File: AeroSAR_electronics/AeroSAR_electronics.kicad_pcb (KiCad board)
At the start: 2 copper layers, 53.5 x 53 mm, 1 part

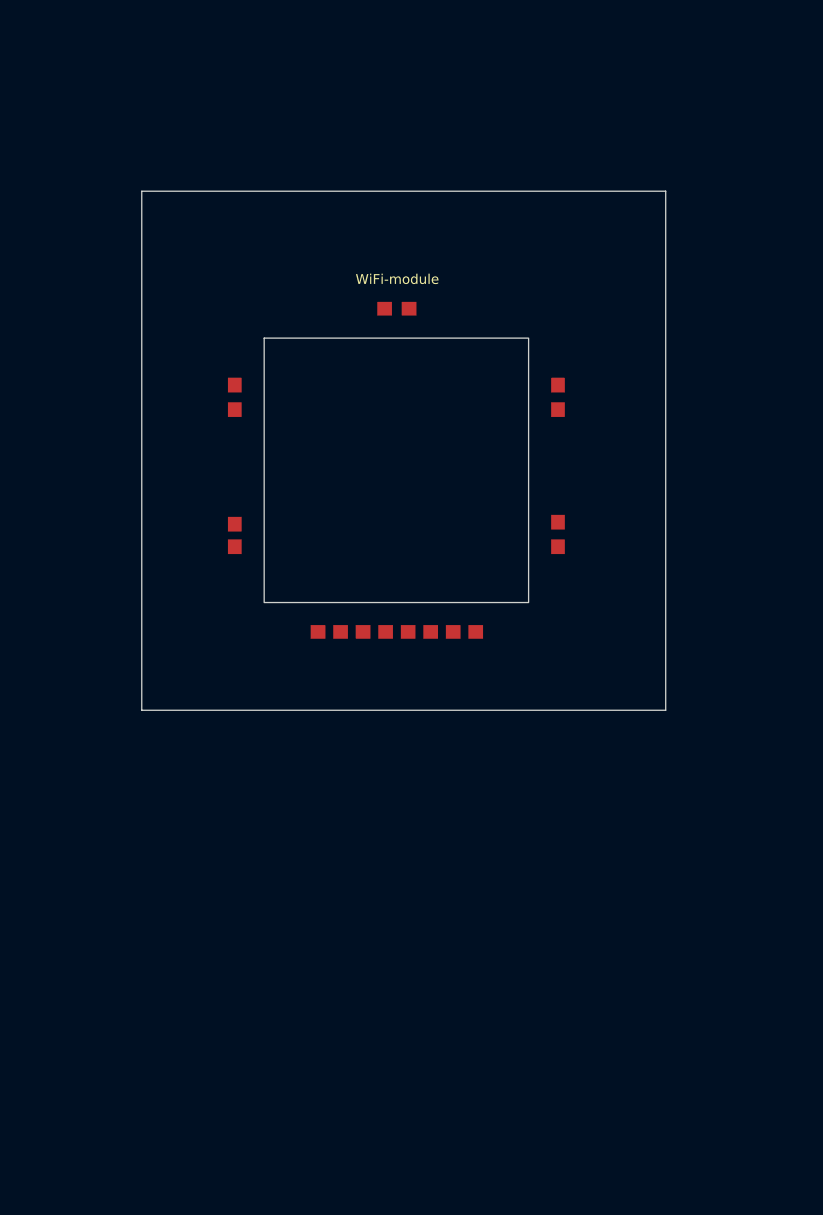
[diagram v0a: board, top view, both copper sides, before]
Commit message: Rearranged the FC-top schematic pins & created a basic pcb outline
Edited the pin type for most of the ground pins
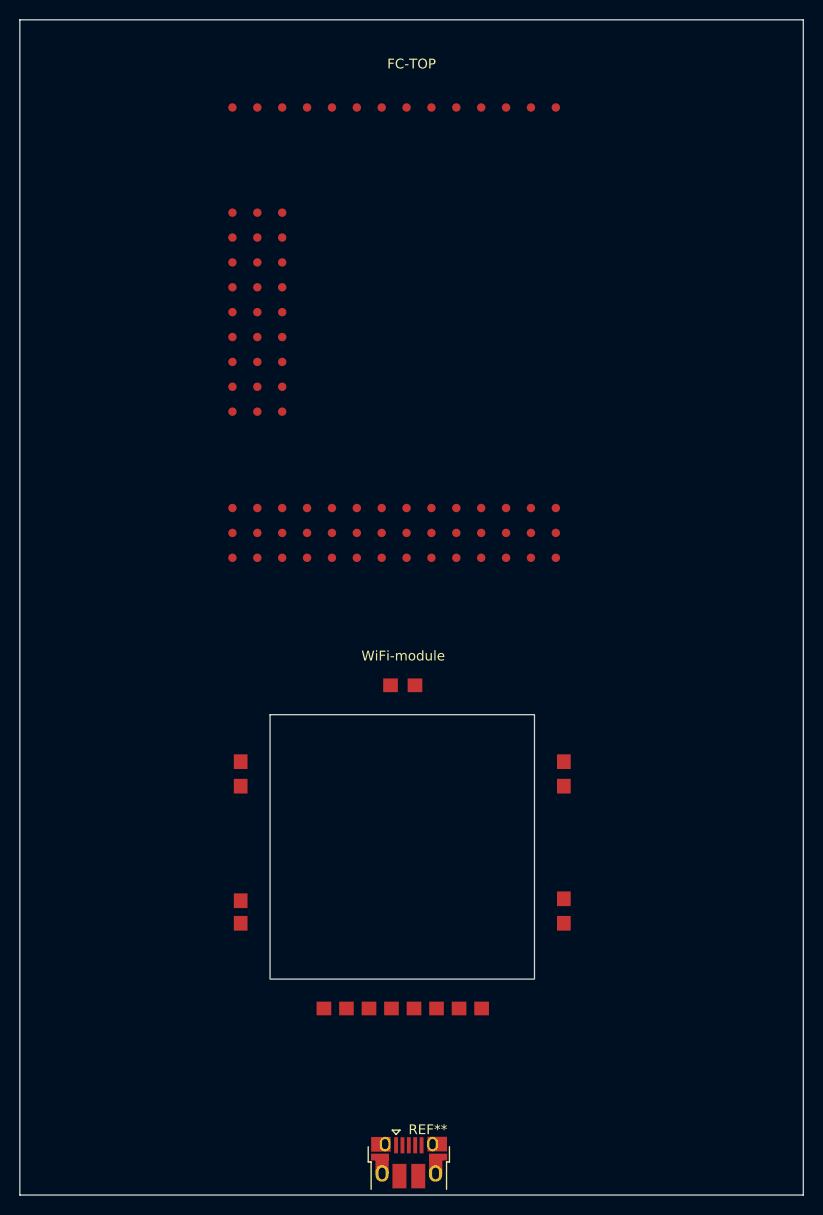
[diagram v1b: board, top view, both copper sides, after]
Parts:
- added FC-TOP: H743-WING-Top, Flight_Controller_Top:H743-WING_TOP, F.Cu at (118.8, 53.9)
- added REF**: USB_Micro-B_Amphenol_10103594-0001LF_Horizontal, Connector_USB:USB_Micro-B_Amphenol_10103594-0001LF_Horizontal, F.Cu at (138.3, 163.2)
- moved WiFi-module 38.5 mm to (121.6, 115.0)
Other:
- board size 53.5 x 53 mm -> 80 x 120 mm

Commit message: Prepared v1 of the schematic
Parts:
- moved REF** 220.0 mm to (357.5, 144.1)
- moved WiFi-module 220.0 mm to (340.8, 95.8)
- moved FC-TOP 220.0 mm to (338.0, 34.8)
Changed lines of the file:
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@@
 	(footprint "Connector_USB:USB_Micro-B_Amphenol_10103594-0001LF_Horizontal"
 		(layer "F.Cu")
-		(at 138.295 163.185)
+		(at 357.495 144.085)
 		(descr "Micro USB Type B 10103594-0001LF, http://cdn.amphenol-icc.com/media/wysiwyg/files/drawing/10103594.pdf")
 		(tags "USB USB_B USB_micro USB_OTG")
@@
 	(footprint "BL-M8812EU2:BL-M8812EU2"
 		(layer "F.Cu")
-		(at 121.6 114.95)
+		(at 340.8 95.85)
 		(property "Reference" "WiFi-module"
 			(at 16.1 -3.5 0)
@@
 	(footprint "Flight_Controller_Top:H743-WING_TOP"
 		(layer "F.Cu")
-		(at 118.8 53.85)
+		(at 338 34.75)
 		(property "Reference" "FC-TOP"
 			(at 19.75 -2.85 0)
@@
 	)
 	(gr_rect
-		(start 98.55 46.5)
-		(end 178.55 166.5)
+		(start 317.75 27.4)
+		(end 397.75 147.4)
 		(stroke
 			(width 0.05)

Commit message: Fixed footprint not loading on schematic and replaced the usb A with usb micro
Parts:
- moved FC-TOP 217.9 mm to (120.4, 46.0)
- moved WiFi-module 217.7 mm to (123.5, 108.5)
- moved REF** 217.7 mm to (140.1, 156.7)
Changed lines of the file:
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@@
 	(footprint "Connector_USB:USB_Micro-B_Amphenol_10103594-0001LF_Horizontal"
 		(layer "F.Cu")
-		(at 357.495 144.085)
+		(at 140.145 156.685)
 		(descr "Micro USB Type B 10103594-0001LF, http://cdn.amphenol-icc.com/media/wysiwyg/files/drawing/10103594.pdf")
 		(tags "USB USB_B USB_micro USB_OTG")
@@
 	(footprint "BL-M8812EU2:BL-M8812EU2"
 		(layer "F.Cu")
-		(at 340.8 95.85)
+		(at 123.45 108.45)
 		(property "Reference" "WiFi-module"
 			(at 16.1 -3.5 0)
@@
 	(footprint "Flight_Controller_Top:H743-WING_TOP"
 		(layer "F.Cu")
-		(at 338 34.75)
+		(at 120.4 46.05)
 		(property "Reference" "FC-TOP"
 			(at 19.75 -2.85 0)
@@
 	)
 	(gr_rect
-		(start 317.75 27.4)
-		(end 397.75 147.4)
+		(start 100.4 40)
+		(end 180.4 160)
 		(stroke
 			(width 0.05)

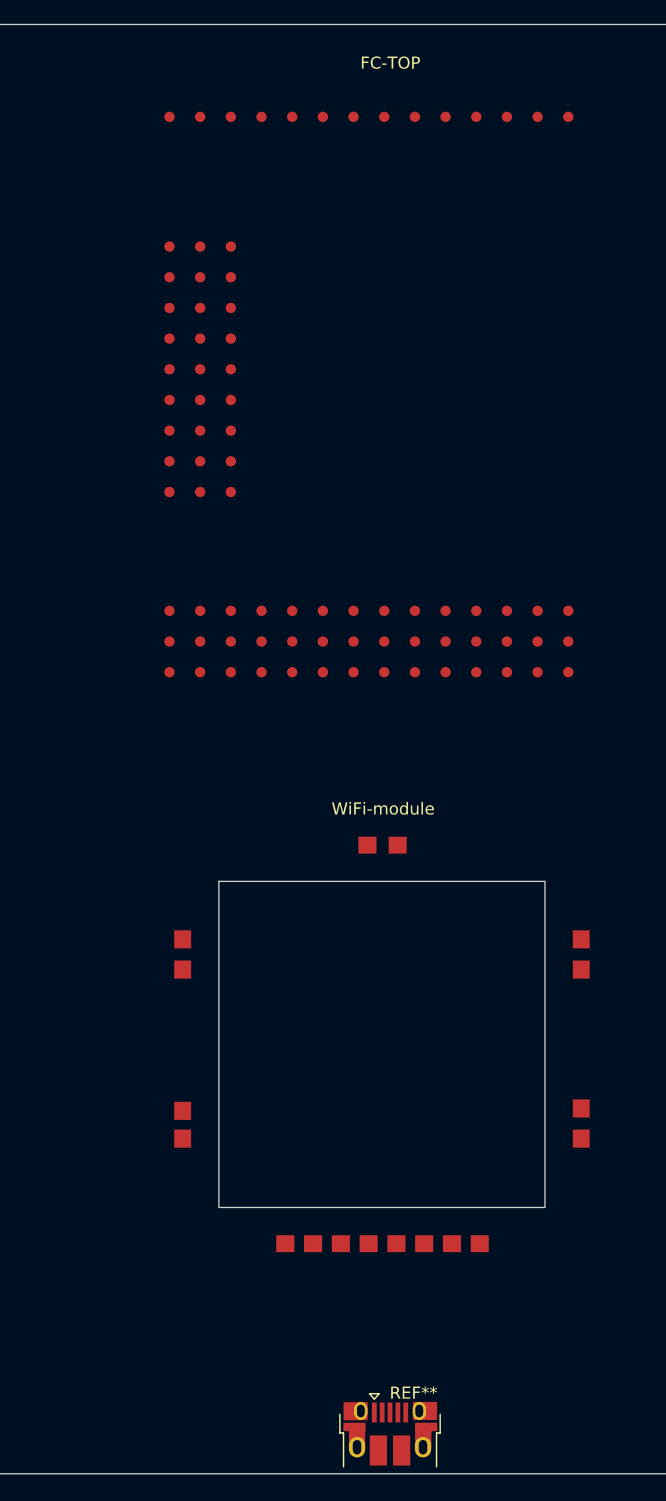
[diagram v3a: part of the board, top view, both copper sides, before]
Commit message: Added usb and power to the PCB
Edited the FC footprint for mounting as well
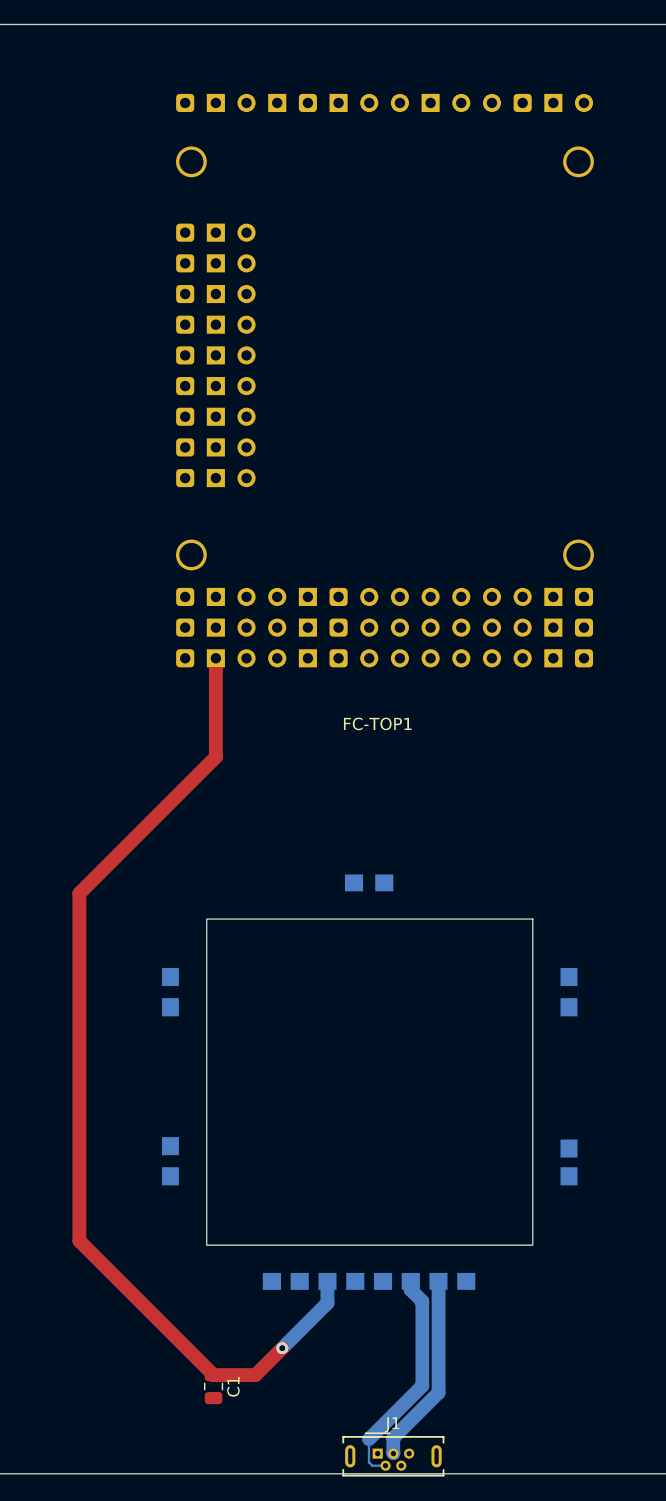
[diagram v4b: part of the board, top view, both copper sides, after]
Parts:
- removed FC-TOP: H743-WING-Top, Flight_Controller_Top:H743-WING_TOP
- removed REF**: USB_Micro-B_Amphenol_10103594-0001LF_Horizontal, Connector_USB:USB_Micro-B_Amphenol_10103594-0001LF_Horizontal
- removed WiFi-module: BL-M8812EU2, BL-M8812EU2:BL-M8812EU2
- added C1: C, Capacitor_SMD:C_0805_2012Metric, F.Cu at (125.5, 152.8)
- added FC-TOP1: ~, Flight_Controller_Top:H743-WING_TOP, F.Cu at (121.7, 44.9)
- added J1: USB_B_Micro, Connector_USB:USB_Micro-B_Wuerth_614105150721_Vertical, F.Cu at (139.1, 158.3)
- added WiFi_module1: ~, BL-M8812EU2:BL-M8812EU2, B.Cu at (154.4, 111.6)
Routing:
- net VCC-WiFi: track 0.00 -> 82.3 mm, vias 0 -> 1
- net Net-(J1-D-): track 0.00 -> 18.4 mm
- net Net-(J1-D+): track 0.00 -> 15.8 mm

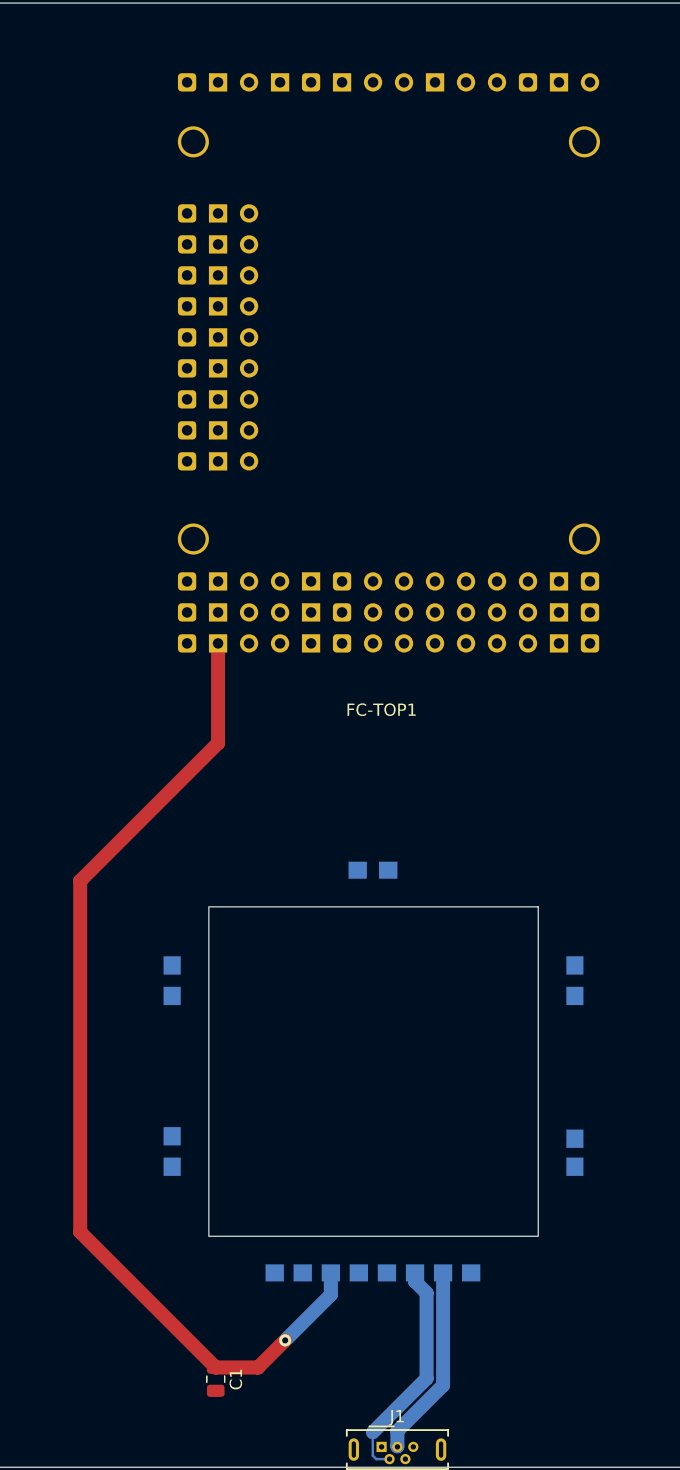
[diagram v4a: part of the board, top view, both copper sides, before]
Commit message: Configured the FC footprint for mounting
Also added another capacitor and moved them closer to the WiFi module
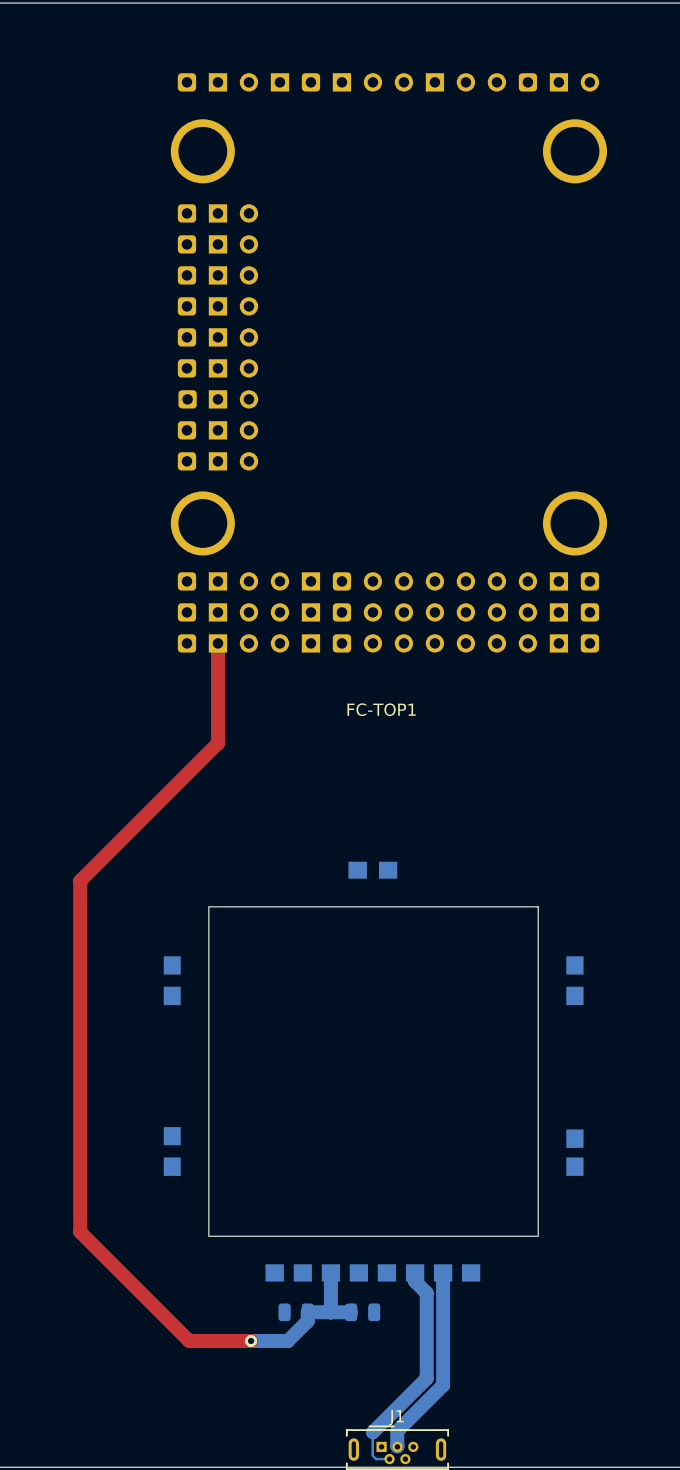
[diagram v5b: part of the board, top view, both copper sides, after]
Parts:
- added C2: C, Capacitor_SMD:C_0805_2012Metric, B.Cu at (132.1, 147.3)
- C1: moved to B.Cu
- moved C1 13.2 mm to (137.6, 147.3), turned to 0 degrees
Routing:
- net VCC-WiFi: track 82.3 -> 83.5 mm
